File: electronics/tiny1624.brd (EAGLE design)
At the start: 26.2 x 16.3 mm, 9 parts, among them U1 ATTINY1624

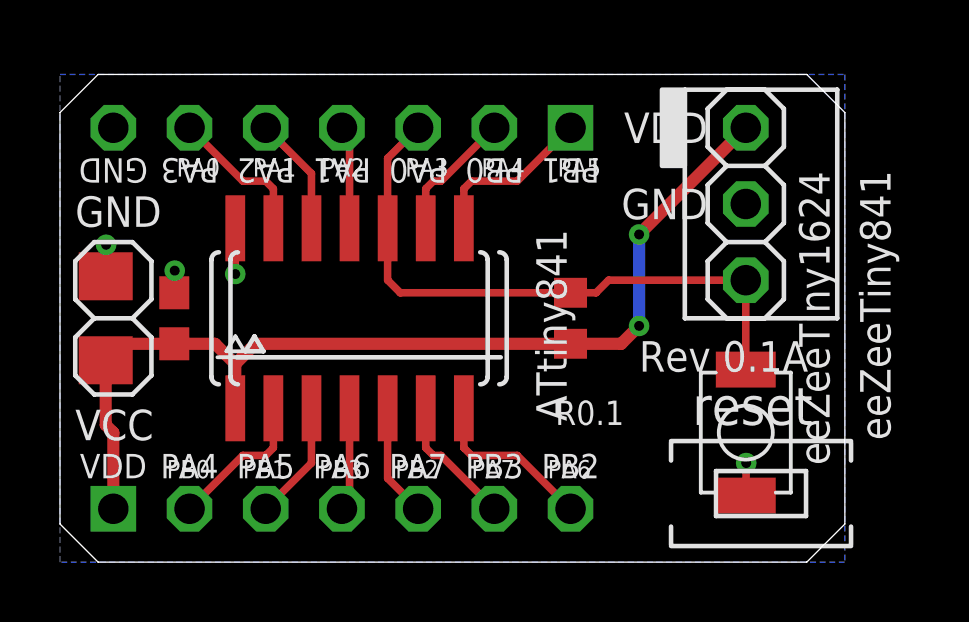
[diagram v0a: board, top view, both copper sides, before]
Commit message: Updated reset circuit, added example blink code
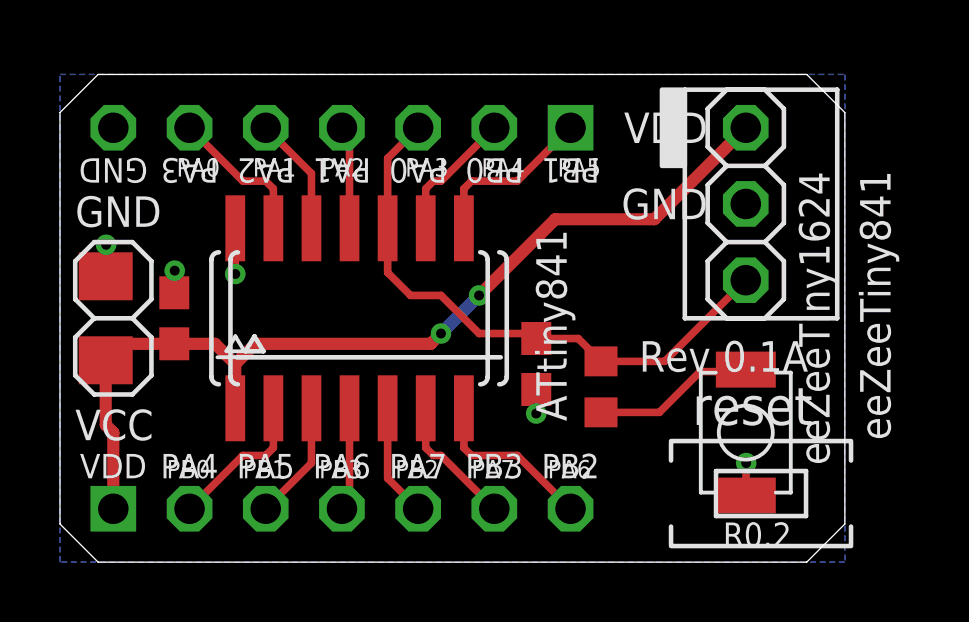
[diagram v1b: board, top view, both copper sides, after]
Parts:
- added C3: 104, bt_rcl:0603
- R1: value 10k -> 330
- moved R1 2.50 mm to (18.0, 5.84), turned to 90 degrees
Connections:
- new net N$12: R1.1, S1.P$2
- net !RESET: now also C3.1, R1.2; no longer R1.1, S1.P$2
- net GND: now also C3.2
- net VCC: no longer R1.2
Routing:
- net N$12: track 0.00 -> 5.42 mm
- net !RESET: track 22.4 -> 19.6 mm
- net VCC: track 33.5 -> 31.7 mm
- net GND: track 4.44 -> 5.25 mm, vias 4 -> 5
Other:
- board text added: "R0.2"
- board text removed: "R0.1"
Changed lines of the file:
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@@
 <setting verticaltext="up"/>
 </settings>
-<grid distance="0.01" unitdist="inch" unit="inch" style="lines" multiple="1" display="no" altdistance="0.1" altunitdist="mm" altunit="mm"/>
+<grid distance="0.005" unitdist="inch" unit="inch" style="lines" multiple="1" display="no" altdistance="0.1" altunitdist="mm" altunit="mm"/>
 <layers>
 <layer number="1" name="Top" color="12" fill="1" visible="yes" active="yes"/>
@@
 <layer number="27" name="tValues" color="7" fill="1" visible="yes" active="yes"/>
 <layer number="28" name="bValues" color="7" fill="1" visible="yes" active="yes"/>
-<layer number="29" name="tStop" color="7" fill="3" visible="no" active="yes"/>
-<layer number="30" name="bStop" color="7" fill="6" visible="no" active="yes"/>
-<layer number="31" name="tCream" color="7" fill="4" visible="no" active="yes"/>
-<layer number="32" name="bCream" color="7" fill="5" visible="no" active="yes"/>
+<layer number="29" name="tStop" color="7" fill="3" visible="yes" active="yes"/>
+<layer number="30" name="bStop" color="7" fill="6" visible="yes" active="yes"/>
+<layer number="31" name="tCream" color="7" fill="4" visible="yes" active="yes"/>
+<layer number="32" name="bCream" color="7" fill="5" visible="yes" active="yes"/>
 <layer number="33" name="tFinish" color="6" fill="3" visible="no" active="yes"/>
 <layer number="34" name="bFinish" color="6" fill="6" visible="no" active="yes"/>
@@
 <wire x1="1.27" y1="16.256" x2="0" y2="14.986" width="0" layer="20"/>
 <text x="6.35" y="4.318" size="0.8128" layer="26" font="vector" ratio="10" rot="MR0" align="bottom-center">bot-thoughts.com</text>
-<text x="16.51" y="4.572" size="0.8128" layer="25" font="vector" ratio="10">R0.1</text>
+<text x="22.098" y="0.508" size="0.8128" layer="25" font="vector" ratio="10">R0.2</text>
 <text x="25.654" y="8.128" size="1.016" layer="25" font="vector" ratio="10" rot="R90" align="bottom-center">eeZeeTiny1624</text>
 <text x="11.938" y="13.462" size="0.8128" layer="25" font="vector" ratio="10" rot="SR180" align="bottom-center">PA0</text>
@@
 <attribute name="VALUE" x="3.81" y="9.779" size="0.8128" layer="27" font="vector" ratio="10" align="bottom-center"/>
 </element>
-<element name="R1" library="rcl" package="R0603" value="10k" x="17.018" y="8.128" smashed="yes" rot="R270">
-<attribute name="PARTNO" value="ERJ-3GEYJ103V" x="17.018" y="8.128" size="1.778" layer="27" rot="R270" display="off"/>
-<attribute name="VALUE" x="17.018" y="9.779" size="0.8128" layer="27" font="vector" ratio="10" align="bottom-center"/>
+<element name="R1" library="rcl" package="R0603" value="330" x="18.034" y="5.842" smashed="yes" rot="R90">
+<attribute name="PARTNO" value="ERJ-3GEYJ103V" x="18.034" y="5.842" size="1.778" layer="27" rot="R90" display="off"/>
+<attribute name="VALUE" x="18.034" y="7.493" size="0.8128" layer="27" font="vector" ratio="10" align="bottom-center"/>
 </element>
 <element name="C2" library="bt_rcl" package="1206" value="106" x="1.524" y="8.128" smashed="yes" rot="R90">
@@
 </element>
 <element name="U$1" library="bt" package="BTLOGOM" value="BTLOGO-LOGO-MD" x="6.35" y="6.604" rot="MR0"/>
-<element name="U1" library="bt_avr" package="SOIC14N" value="ATTINY1624" x="9.652" y="8.128" smashed="yes">
-<attribute name="VALUE" x="14.478" y="8.382" size="0.8128" layer="27" font="vector" ratio="10" rot="R270" align="bottom-center"/>
-</element>
+<element name="U1" library="bt_avr" package="SOIC14N" value="ATTINY1624" x="9.652" y="8.128" smashed="yes"/>
 <element name="JP2" library="pinhead-2" package="1X03-S" value="UPDI" x="22.86" y="11.938" smashed="yes" rot="R90">
 <attribute name="VALUE" x="21.59" y="9.779" size="1.016" layer="27" font="vector" ratio="10" rot="R180"/>
+</element>
+<element name="C3" library="bt_rcl" package="0603" value="104" x="15.875" y="6.604" smashed="yes" rot="R270">
+<attribute name="PARTNO" value="0603YC104KAT2A" x="15.875" y="6.604" size="1.778" layer="27" rot="R270" display="off"/>
+<attribute name="BOM" value="EXCLUDE" x="15.875" y="6.604" size="1.778" layer="27" rot="R270" display="off"/>
+<attribute name="VALUE" x="15.875" y="8.382" size="0.8128" layer="27" font="vector" ratio="10" rot="R180" align="top-center"/>
 </element>
 </elements>
@@
 <via x="5.842" y="9.604" extent="1-16" drill="0.3302"/>
 <wire x1="5.842" y1="11.128" x2="5.842" y2="11.176" width="0.254" layer="1"/>
+<contactref element="C3" pad="2"/>
+<wire x1="15.875" y1="5.754" x2="15.875" y2="4.953" width="0.254" layer="1"/>
+<via x="15.875" y="4.953" extent="1-16" drill="0.3302"/>
 </signal>
 <signal name="VCC">
 <contactref element="C1" pad="1"/>
-<contactref element="R1" pad="2"/>
 <contactref element="C2" pad="1"/>
 <contactref element="JP4" pad="1"/>
@@
 <wire x1="5.168" y1="7.278" x2="5.842" y2="6.604" width="0.4064" layer="1"/>
 <wire x1="5.842" y1="6.604" x2="5.842" y2="5.128" width="0.4064" layer="1"/>
-<wire x1="17.018" y1="7.278" x2="6.516" y2="7.278" width="0.4064" layer="1"/>
 <wire x1="6.516" y1="7.278" x2="5.842" y2="6.604" width="0.4064" layer="1"/>
-<wire x1="17.018" y1="7.278" x2="18.708" y2="7.278" width="0.4064" layer="1"/>
-<wire x1="18.708" y1="7.278" x2="19.304" y2="7.874" width="0.4064" layer="1"/>
-<via x="19.304" y="7.874" extent="1-16" drill="0.3302"/>
-<wire x1="19.304" y1="7.874" x2="19.304" y2="10.922" width="0.4064" layer="16"/>
-<via x="19.304" y="10.922" extent="1-16" drill="0.3302"/>
-<wire x1="19.304" y1="10.922" x2="22.86" y2="14.478" width="0.4064" layer="1"/>
+<wire x1="6.516" y1="7.278" x2="12.358" y2="7.278" width="0.4064" layer="1"/>
+<wire x1="12.358" y1="7.278" x2="12.7" y2="7.62" width="0.4064" layer="1"/>
+<via x="12.7" y="7.62" extent="1-16" drill="0.3302"/>
+<wire x1="12.7" y1="7.62" x2="13.97" y2="8.89" width="0.4064" layer="16"/>
+<via x="13.97" y="8.89" extent="1-16" drill="0.3302"/>
+<wire x1="13.97" y1="8.89" x2="16.51" y2="11.43" width="0.4064" layer="1"/>
+<wire x1="16.51" y1="11.43" x2="19.812" y2="11.43" width="0.4064" layer="1"/>
+<wire x1="19.812" y1="11.43" x2="22.86" y2="14.478" width="0.4064" layer="1"/>
 </signal>
 <signal name="!RESET">
-<contactref element="R1" pad="1"/>
-<contactref element="S1" pad="P$2"/>
 <contactref element="U1" pad="10"/>
 <contactref element="JP5" pad="3"/>
 <contactref element="JP2" pad="1"/>
-<wire x1="22.86" y1="6.418" x2="23.69" y2="6.028" width="0.254" layer="1"/>
-<wire x1="23.69" y1="6.028" x2="22.86" y2="6.858" width="0.254" layer="1"/>
-<wire x1="22.86" y1="6.858" x2="22.86" y2="9.398" width="0.254" layer="1"/>
-<wire x1="17.018" y1="8.978" x2="17.868" y2="8.978" width="0.254" layer="1"/>
-<wire x1="17.868" y1="8.978" x2="18.288" y2="9.398" width="0.254" layer="1"/>
-<wire x1="18.288" y1="9.398" x2="22.86" y2="9.398" width="0.254" layer="1"/>
 <wire x1="10.922" y1="11.128" x2="10.922" y2="13.462" width="0.254" layer="1"/>
 <wire x1="10.922" y1="13.462" x2="11.938" y2="14.478" width="0.254" layer="1"/>
-<wire x1="17.018" y1="8.978" x2="11.342" y2="8.978" width="0.254" layer="1"/>
-<wire x1="11.342" y1="8.978" x2="10.922" y2="9.398" width="0.254" layer="1"/>
-<wire x1="10.922" y1="9.398" x2="10.922" y2="11.128" width="0.254" layer="1"/>
+<wire x1="11.684" y1="8.89" x2="10.922" y2="9.652" width="0.254" layer="1"/>
+<wire x1="10.922" y1="9.652" x2="10.922" y2="11.128" width="0.254" layer="1"/>
+<contactref element="R1" pad="2"/>
+<contactref element="C3" pad="1"/>
+<wire x1="12.7" y1="8.89" x2="11.684" y2="8.89" width="0.254" layer="1"/>
+<wire x1="12.7" y1="8.89" x2="13.97" y2="7.62" width="0.254" layer="1"/>
+<wire x1="13.97" y1="7.62" x2="15.836" y2="7.62" width="0.254" layer="1"/>
+<wire x1="15.836" y1="7.62" x2="15.875" y2="7.454" width="0.254" layer="1"/>
+<wire x1="15.875" y1="7.454" x2="17.272" y2="7.454" width="0.254" layer="1"/>
+<wire x1="17.272" y1="7.454" x2="18.034" y2="6.692" width="0.254" layer="1"/>
+<wire x1="18.034" y1="6.692" x2="20.154" y2="6.692" width="0.254" layer="1"/>
+<wire x1="20.154" y1="6.692" x2="22.86" y2="9.398" width="0.254" layer="1"/>
 </signal>
 <signal name="N$1">
@@
 <wire x1="6.096" y1="12.7" x2="4.318" y2="14.478" width="0.254" layer="1"/>
 </signal>
+<signal name="N$12">
+<contactref element="R1" pad="1"/>
+<contactref element="S1" pad="P$2"/>
+<wire x1="18.034" y1="4.992" x2="19.978" y2="4.992" width="0.254" layer="1"/>
+<wire x1="19.978" y1="4.992" x2="21.336" y2="6.35" width="0.254" layer="1"/>
+<wire x1="21.336" y1="6.35" x2="22.792" y2="6.35" width="0.254" layer="1"/>
+<wire x1="22.792" y1="6.35" x2="22.86" y2="6.418" width="0.254" layer="1"/>
+</signal>
 </signals>

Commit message: Removed reset circuit, shrunk board, cleaned up schematic
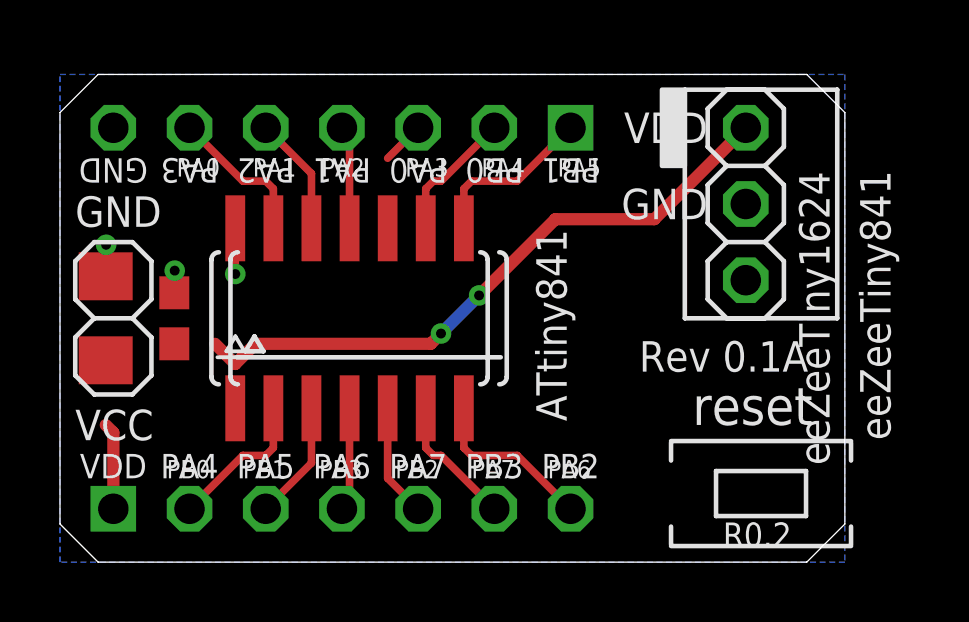
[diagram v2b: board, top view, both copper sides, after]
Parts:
- removed C3: 104, bt_rcl:0603
- removed R1: 330, rcl:R0603
- removed S1: reset, bt_electromech:3X4X2TACT
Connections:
- removed net !RESET: C3.1, JP2.1, JP5.3, R1.2, U1.10
- removed net N$12: R1.1, S1.P$2
- new net UPDI: JP2.1, JP5.3, U1.10
- net GND: no longer C3.2, S1.P$1
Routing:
- net !RESET: track 19.6 -> 0.00 mm
- net VCC: track 31.7 -> 24.1 mm
- net N$12: track 5.42 -> 0.00 mm
- net GND: track 5.25 -> 3.36 mm, vias 5 -> 3
- net UPDI: track 0.00 -> 1.44 mm
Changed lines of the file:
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@@
 <attribute name="VALUE" x="3.81" y="9.779" size="0.8128" layer="27" font="vector" ratio="10" align="bottom-center"/>
-</element>
-<element name="R1" library="rcl" package="R0603" value="330" x="18.034" y="5.842" smashed="yes" rot="R90">
-<attribute name="PARTNO" value="ERJ-3GEYJ103V" x="18.034" y="5.842" size="1.778" layer="27" rot="R90" display="off"/>
-<attribute name="VALUE" x="18.034" y="7.493" size="0.8128" layer="27" font="vector" ratio="10" align="bottom-center"/>
 </element>
 <element name="C2" library="bt_rcl" package="1206" value="106" x="1.524" y="8.128" smashed="yes" rot="R90">
@@
 <attribute name="VALUE" x="18.288" y="11.303" size="1.27" layer="28" rot="MR0"/>
 </element>
-<element name="S1" library="bt_electromech" package="3X4X2TACT" value="reset" x="22.86" y="4.318" smashed="yes" rot="R90">
-<attribute name="VALUE" x="21.082" y="4.318" size="1.27" layer="27" font="vector" ratio="10" rot="R90" align="bottom-center"/>
-</element>
 <element name="U$1" library="bt" package="BTLOGOM" value="BTLOGO-LOGO-MD" x="6.35" y="6.604" rot="MR0"/>
 <element name="U1" library="bt_avr" package="SOIC14N" value="ATTINY1624" x="9.652" y="8.128" smashed="yes"/>
 <element name="JP2" library="pinhead-2" package="1X03-S" value="UPDI" x="22.86" y="11.938" smashed="yes" rot="R90">
 <attribute name="VALUE" x="21.59" y="9.779" size="1.016" layer="27" font="vector" ratio="10" rot="R180"/>
-</element>
-<element name="C3" library="bt_rcl" package="0603" value="104" x="15.875" y="6.604" smashed="yes" rot="R270">
-<attribute name="PARTNO" value="0603YC104KAT2A" x="15.875" y="6.604" size="1.778" layer="27" rot="R270" display="off"/>
-<attribute name="BOM" value="EXCLUDE" x="15.875" y="6.604" size="1.778" layer="27" rot="R270" display="off"/>
-<attribute name="VALUE" x="15.875" y="8.382" size="0.8128" layer="27" font="vector" ratio="10" rot="R180" align="top-center"/>
 </element>
 </elements>
@@
 </polygon>
 <contactref element="JP5" pad="7"/>
-<contactref element="S1" pad="P$1"/>
 <contactref element="C2" pad="2"/>
 <contactref element="U1" pad="14"/>
-<contactref element="JP2" pad="2"/>
 <wire x1="1.524" y1="9.528" x2="1.5376" y2="10.5782" width="0.254" layer="1"/>
 <wire x1="3.81" y1="8.978" x2="3.8236" y2="9.7164" width="0.254" layer="1"/>
 <via x="3.8236" y="9.7164" extent="1-16" drill="0.3302"/>
 <via x="1.5376" y="10.5782" extent="1-16" drill="0.3302"/>
-<via x="22.8736" y="3.302" extent="1-16" drill="0.3302"/>
-<wire x1="22.86" y1="2.218" x2="22.8736" y2="3.302" width="0.254" layer="1"/>
 <wire x1="5.842" y1="9.604" x2="5.842" y2="11.128" width="0.254" layer="1"/>
 <via x="5.842" y="9.604" extent="1-16" drill="0.3302"/>
 <wire x1="5.842" y1="11.128" x2="5.842" y2="11.176" width="0.254" layer="1"/>
-<contactref element="C3" pad="2"/>
-<wire x1="15.875" y1="5.754" x2="15.875" y2="4.953" width="0.254" layer="1"/>
-<via x="15.875" y="4.953" extent="1-16" drill="0.3302"/>
+<contactref element="JP2" pad="2"/>
 </signal>
 <signal name="VCC">
-<contactref element="C1" pad="1"/>
-<contactref element="C2" pad="1"/>
 <contactref element="JP4" pad="1"/>
-<contactref element="U1" pad="1"/>
 <contactref element="JP2" pad="3"/>
-<wire x1="3.81" y1="7.278" x2="1.82" y2="7.278" width="0.4064" layer="1"/>
-<wire x1="1.82" y1="7.278" x2="1.524" y2="6.728" width="0.4064" layer="1"/>
 <wire x1="1.778" y1="1.778" x2="1.778" y2="4.318" width="0.4064" layer="1"/>
 <wire x1="1.778" y1="4.318" x2="1.524" y2="4.572" width="0.4064" layer="1"/>
-<wire x1="1.524" y1="4.572" x2="1.524" y2="6.728" width="0.4064" layer="1"/>
-<wire x1="3.81" y1="7.278" x2="5.168" y2="7.278" width="0.4064" layer="1"/>
 <wire x1="5.168" y1="7.278" x2="5.842" y2="6.604" width="0.4064" layer="1"/>
-<wire x1="5.842" y1="6.604" x2="5.842" y2="5.128" width="0.4064" layer="1"/>
 <wire x1="6.516" y1="7.278" x2="5.842" y2="6.604" width="0.4064" layer="1"/>
 <wire x1="6.516" y1="7.278" x2="12.358" y2="7.278" width="0.4064" layer="1"/>
@@
 <wire x1="16.51" y1="11.43" x2="19.812" y2="11.43" width="0.4064" layer="1"/>
 <wire x1="19.812" y1="11.43" x2="22.86" y2="14.478" width="0.4064" layer="1"/>
-</signal>
-<signal name="!RESET">
-<contactref element="U1" pad="10"/>
-<contactref element="JP5" pad="3"/>
-<contactref element="JP2" pad="1"/>
-<wire x1="10.922" y1="11.128" x2="10.922" y2="13.462" width="0.254" layer="1"/>
-<wire x1="10.922" y1="13.462" x2="11.938" y2="14.478" width="0.254" layer="1"/>
-<wire x1="11.684" y1="8.89" x2="10.922" y2="9.652" width="0.254" layer="1"/>
-<wire x1="10.922" y1="9.652" x2="10.922" y2="11.128" width="0.254" layer="1"/>
-<contactref element="R1" pad="2"/>
-<contactref element="C3" pad="1"/>
-<wire x1="12.7" y1="8.89" x2="11.684" y2="8.89" width="0.254" layer="1"/>
-<wire x1="12.7" y1="8.89" x2="13.97" y2="7.62" width="0.254" layer="1"/>
-<wire x1="13.97" y1="7.62" x2="15.836" y2="7.62" width="0.254" layer="1"/>
-<wire x1="15.836" y1="7.62" x2="15.875" y2="7.454" width="0.254" layer="1"/>
-<wire x1="15.875" y1="7.454" x2="17.272" y2="7.454" width="0.254" layer="1"/>
-<wire x1="17.272" y1="7.454" x2="18.034" y2="6.692" width="0.254" layer="1"/>
-<wire x1="18.034" y1="6.692" x2="20.154" y2="6.692" width="0.254" layer="1"/>
-<wire x1="20.154" y1="6.692" x2="22.86" y2="9.398" width="0.254" layer="1"/>
+<contactref element="C1" pad="1"/>
+<contactref element="U1" pad="1"/>
+<contactref element="C2" pad="1"/>
+<wire x1="3.81" y1="7.278" x2="5.168" y2="7.278" width="0" layer="19" extent="1-1"/>
+<wire x1="5.842" y1="5.128" x2="5.842" y2="6.604" width="0" layer="19" extent="1-1"/>
+<wire x1="1.524" y1="6.728" x2="3.81" y2="7.278" width="0" layer="19" extent="1-1"/>
+<wire x1="1.524" y1="4.572" x2="1.524" y2="6.728" width="0" layer="19" extent="1-1"/>
 </signal>
 <signal name="N$1">
@@
 <wire x1="6.096" y1="12.7" x2="4.318" y2="14.478" width="0.254" layer="1"/>
 </signal>
-<signal name="N$12">
-<contactref element="R1" pad="1"/>
-<contactref element="S1" pad="P$2"/>
-<wire x1="18.034" y1="4.992" x2="19.978" y2="4.992" width="0.254" layer="1"/>
-<wire x1="19.978" y1="4.992" x2="21.336" y2="6.35" width="0.254" layer="1"/>
-<wire x1="21.336" y1="6.35" x2="22.792" y2="6.35" width="0.254" layer="1"/>
-<wire x1="22.792" y1="6.35" x2="22.86" y2="6.418" width="0.254" layer="1"/>
+<signal name="UPDI">
+<contactref element="U1" pad="10"/>
+<contactref element="JP2" pad="1"/>
+<contactref element="JP5" pad="3"/>
+<wire x1="10.922" y1="13.462" x2="11.938" y2="14.478" width="0.254" layer="1"/>
+<wire x1="11.938" y1="14.478" x2="22.86" y2="9.398" width="0" layer="19" extent="1-1"/>
+<wire x1="10.922" y1="11.128" x2="10.922" y2="13.462" width="0" layer="19" extent="1-1"/>
 </signal>
 </signals>

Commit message: Added arduino labeling
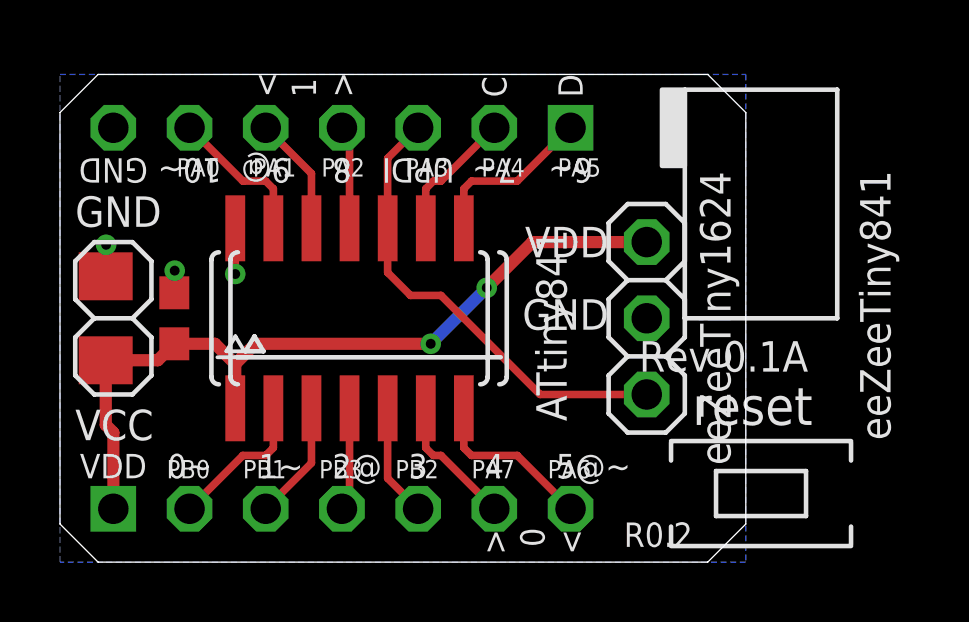
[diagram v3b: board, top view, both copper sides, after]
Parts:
- moved JP2 5.04 mm to (19.6, 8.13)
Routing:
- net UPDI: track 1.44 -> 15.6 mm
- net VCC: track 24.1 -> 26.8 mm
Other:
- board size 26.2 x 16.3 mm -> 22.9 x 16.3 mm
- board text added: "0"
- board text added: "0~"
- board text added: "1"
- board text added: "10~"
- board text added: "1~"
- board text added: "2@"
- board text added: "3"
- board text added: "4"
- board text added: "5@~"
- board text added: "6~"
- board text added: "7~"
- board text added: "8"
- board text added: "9@"
- board text added: "<"
- board text added: ">"
- board text added: "C"
- board text added: "D"
- board text added: "UPDI"
- board text added: "cc-by-sa"
- board text added: "is.gd/ssuwHj"
- board text added: "~ PWM @ ASYNC <> UART C SCL D SDA"
- board text removed: "CC-BY-SA"
